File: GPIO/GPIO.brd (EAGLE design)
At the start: 25.4 x 25.4 mm, 11 parts

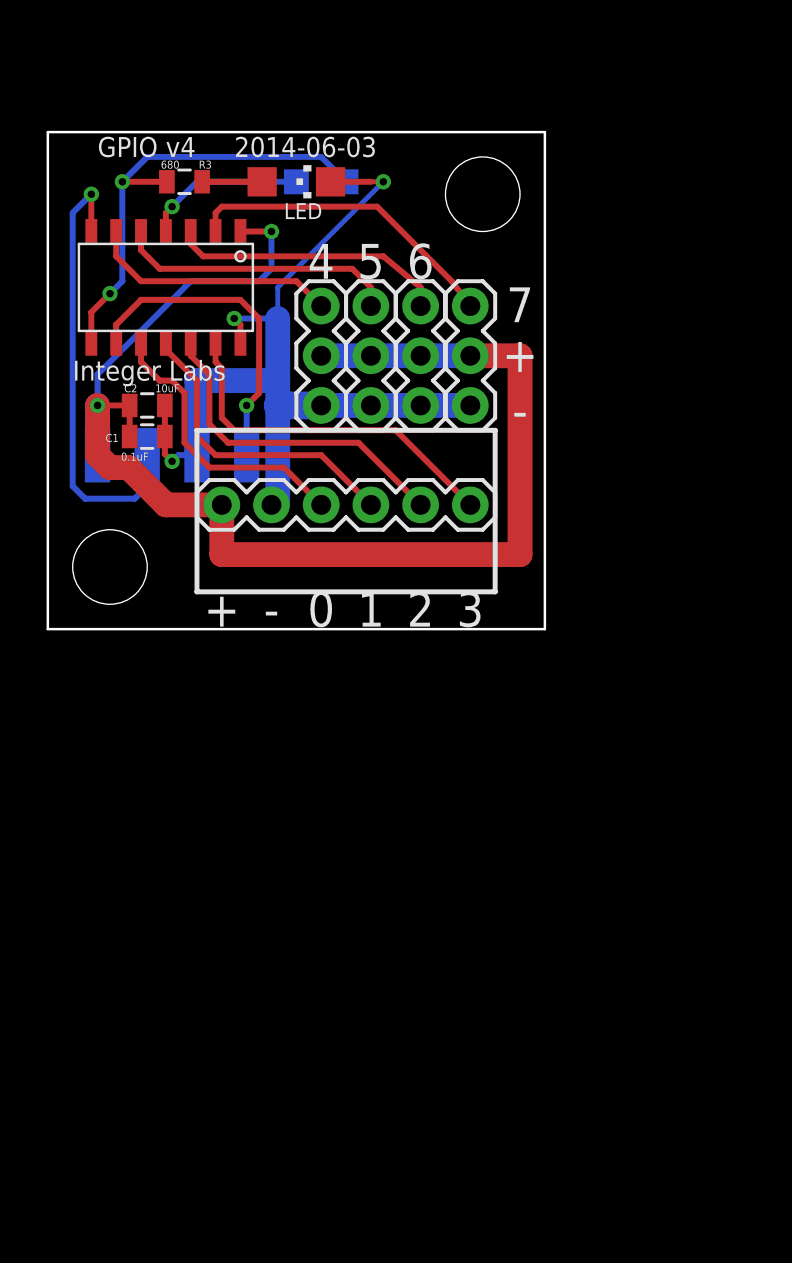
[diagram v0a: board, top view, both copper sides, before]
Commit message: GPIO board rebuilt for v2 footprint
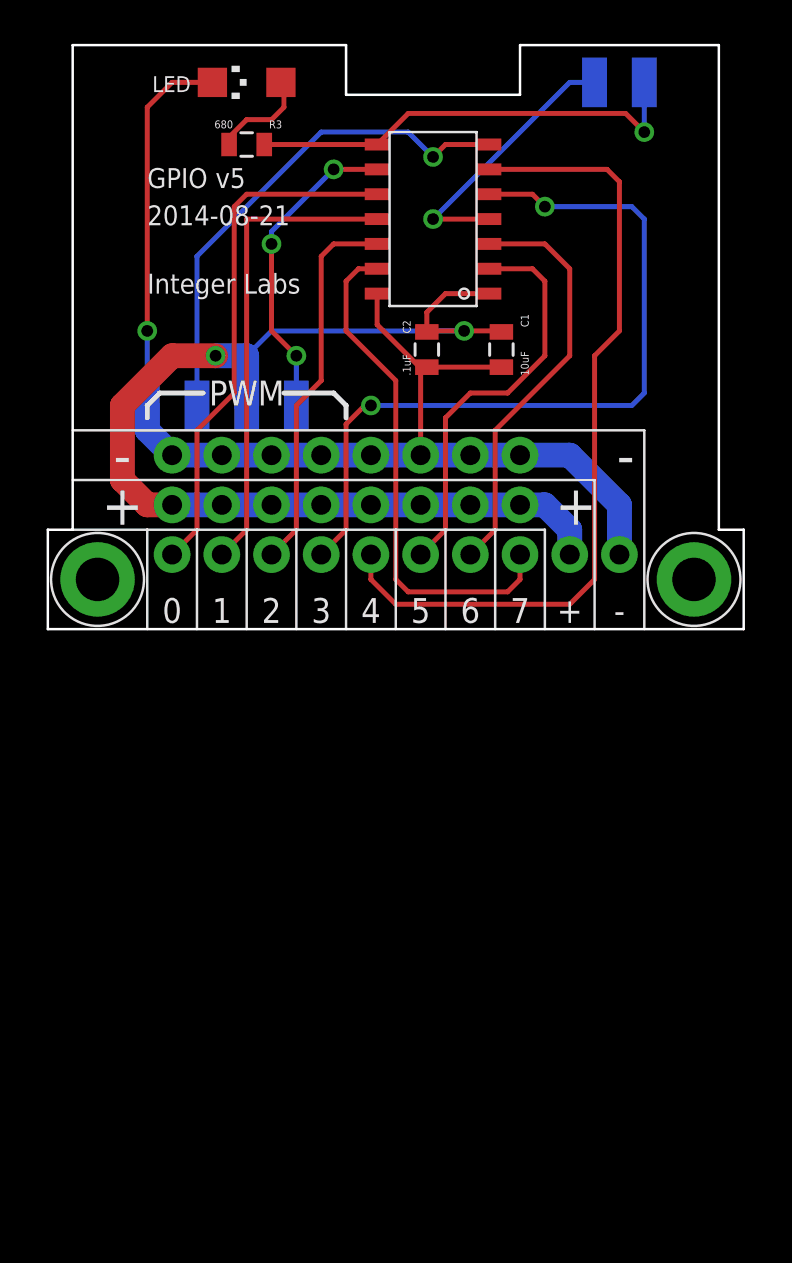
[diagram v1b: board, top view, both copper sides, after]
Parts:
- removed JP5, JP6, JP7, JP8: (no value), SparkFun-Connectors:1X03
- added JP1, JP3: (no value), SparkFun-Connectors:1X08_NO_SILK
- C1: value 0.1uF -> 10uF
- C2: value 10uF -> .1uF
- JP2: value (none) -> M10NO_SILK; device SparkFun-Connectors:1X06 -> SparkFun-Connectors:1X10_NO_SILK
- U$4: value FOOTPRINT -> FOOTPRINTFOOTPRINT-2; device IntegerLabs:FOOTPRINT -> IntegerLabs:FOOTPRINT2
- moved C1 18.6 mm to (23.2, 14.3), turned to 90 degrees
- moved C2 14.6 mm to (19.4, 14.3), turned to 90 degrees
- moved U$3 9.53 mm to (19.4, 17.1), turned to 90 degrees
- moved LED 5.68 mm to (10.2, 27.9), turned to 90 degrees
- moved R3 3.70 mm to (10.2, 24.8), turned to 0 degrees
- moved JP2 3.59 mm to (6.35, 3.81)
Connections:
- net GND: now also JP1.1, JP1.2, JP1.3, JP1.4, JP1.5, JP1.6, JP1.7, JP1.8, JP2.10, U$4.GND; no longer JP2.2, JP5.3, JP6.3, JP7.3, JP8.3, U$4.P$3
- net GPIO0: now also JP2.1; no longer JP2.3
- net GPIO1: now also JP2.2; no longer JP2.4
- net GPIO2: now also JP2.3; no longer JP2.5
- net GPIO3: now also JP2.4, U$3.5; no longer JP2.6, U$3.13
- net GPIO4: now also JP2.5; no longer JP5.1
- net GPIO5: now also JP2.6, U$3.2; no longer JP6.1, U$3.5
- net GPIO6: now also JP2.7; no longer JP7.1
- net GPIO7: now also JP2.8, U$3.13; no longer JP8.1, U$3.2
- net SCL/SCK: now also U$4.SCL; no longer U$4.P$4
- net SDA/MOSI: now also U$4.SDA; no longer U$4.P$2
- net VCC: now also JP2.9, JP3.1, JP3.2, JP3.3, JP3.4, JP3.5, JP3.6, JP3.7, JP3.8, U$4.VCC; no longer JP2.1, JP5.2, JP6.2, JP7.2, JP8.2, U$4.P$1
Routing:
- net GPIO4: track 12.8 -> 41.5 mm
- net GPIO3: track 18.5 -> 40.4 mm, vias 0 -> 2
- net GND: track 47.4 -> 62.1 mm, vias 3 -> 1
- net GPIO0: track 14.7 -> 26.7 mm
- net VCC: track 70.0 -> 59.0 mm
- net GPIO7: track 16.3 -> 26.3 mm
- net GPIO1: track 15.8 -> 24.3 mm
- net GPIO6: track 14.2 -> 21.4 mm
- net GPIO5: track 14.4 -> 20.8 mm
- net RESET: track 8.28 -> 14.0 mm
- net SDA/MOSI: track 23.1 -> 26.0 mm
- net GPIO2: track 17.0 -> 19.4 mm
- net N$5: track 3.06 -> 5.15 mm
- net MISO/LED: track 23.7 -> 23.0 mm, vias 2 -> 1
- net SCL/SCK: track 16.4 -> 16.1 mm, vias 1 -> 3
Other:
- board size 25.4 x 25.4 mm -> 35.6 x 29.8 mm
- board text added: "2014-08-21"
- board text added: "GPIO v5"
- board text added: "PWM"
- board text removed: "2014-06-03"
- board text removed: "GPIO v4"

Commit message: Added current limiting resistors to io pins
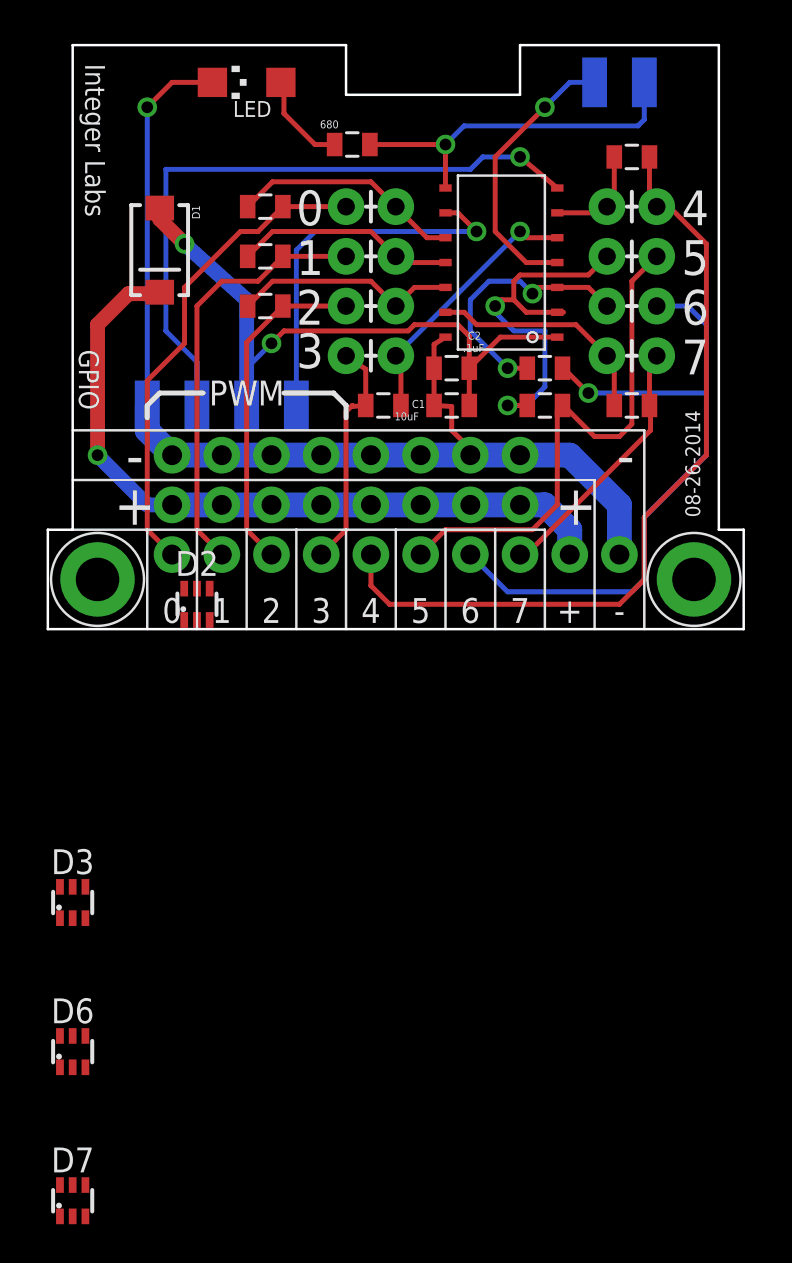
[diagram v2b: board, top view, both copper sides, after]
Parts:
- removed R3: 680, SparkFun-Passives:0805
- added D1: DIODE-SCHOTTKY_, SparkFun-DiscreteSemi:SMA-DIODE
- added D2, D3, D6, D7: BAS70XY, diode:SOT363_PHILIPS
- added R0A, R1A, R2A, R3A, R4A, R5A, R6A, R7A: (no value), SparkFun-Resistors:AXIAL-0.1
- added R0B, R1B, R2B, R3B, R4B, R5B, R6B, R7B: (no value), SparkFun-Resistors:0805
- added RLED: 680, SparkFun-Passives:0805
- moved U$3 4.14 mm to (22.9, 14.9)
- moved C2 3.13 mm to (20.6, 11.4), turned to 0 degrees
- moved C1 2.71 mm to (20.6, 13.3), turned to 0 degrees
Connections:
- new net N$1: D2.2, D6.6
- new net N$2: D2.5, D6.3
- new net N$3: D3.2, D7.6
- new net P0: JP2.1, R0A.P$2, R0B.2
- new net P1: JP2.2, R1A.P$2, R1B.2
- new net P2: JP2.3, R2A.P$2, R2B.2
- new net P3: JP2.4, R3A.P$2, R3B.2
- new net P4: JP2.5, R4A.P$1, R4B.1
- new net P5: JP2.6, R5A.P$1, R5B.1
- new net P6: JP2.7, R6A.P$1, R6B.1
- new net P7: JP2.8, R7A.P$1, R7B.1
- new net VOUT: D1.C, JP2.9, JP3.1, JP3.2, JP3.3, JP3.4, JP3.5, JP3.6, JP3.7, JP3.8
- net GPIO0: now also R0A.P$1, R0B.1; no longer JP2.1
- net GPIO1: now also R1A.P$1, R1B.1; no longer JP2.2
- net GPIO2: now also R2A.P$1, R2B.1; no longer JP2.3
- net GPIO3: now also R3A.P$1, R3B.1; no longer JP2.4
- net GPIO4: now also R4A.P$2, R4B.2; no longer JP2.5
- net GPIO5: now also R5A.P$2, R5B.2; no longer JP2.6
- net GPIO6: now also R6A.P$2, R6B.2; no longer JP2.7
- net GPIO7: now also R7A.P$2, R7B.2; no longer JP2.8
- net MISO/LED: now also RLED.2; no longer R3.2
- net N$5: now also RLED.1; no longer R3.1
- net VCC: now also D1.A; no longer JP2.9, JP3.1, JP3.2, JP3.3, JP3.4, JP3.5, JP3.6, JP3.7, JP3.8
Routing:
- net P4: track 0.00 -> 41.0 mm
- net VOUT: track 0.00 -> 37.5 mm, vias 0 -> 1
- net GPIO4: track 41.5 -> 5.36 mm
- net P6: track 0.00 -> 35.1 mm, vias 0 -> 1
- net GPIO3: track 40.4 -> 13.6 mm, vias 2 -> 1
- net P5: track 0.00 -> 26.8 mm
- net P0: track 0.00 -> 24.9 mm
- net VCC: track 59.0 -> 35.2 mm
- net P1: track 0.00 -> 21.9 mm
- net P2: track 0.00 -> 17.2 mm
- net GPIO0: track 26.7 -> 11.8 mm
- net GPIO7: track 26.3 -> 11.9 mm
- net P7: track 0.00 -> 13.3 mm
- net GPIO1: track 24.3 -> 11.3 mm
- net P3: track 0.00 -> 12.1 mm
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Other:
- board text added: "08-26-2014"
- board text added: "GPIO"
- board text removed: "2014-08-21"
- board text removed: "GPIO v5"

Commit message: Ruggedized GPIO board with current limiting resistors and clamping diodes.
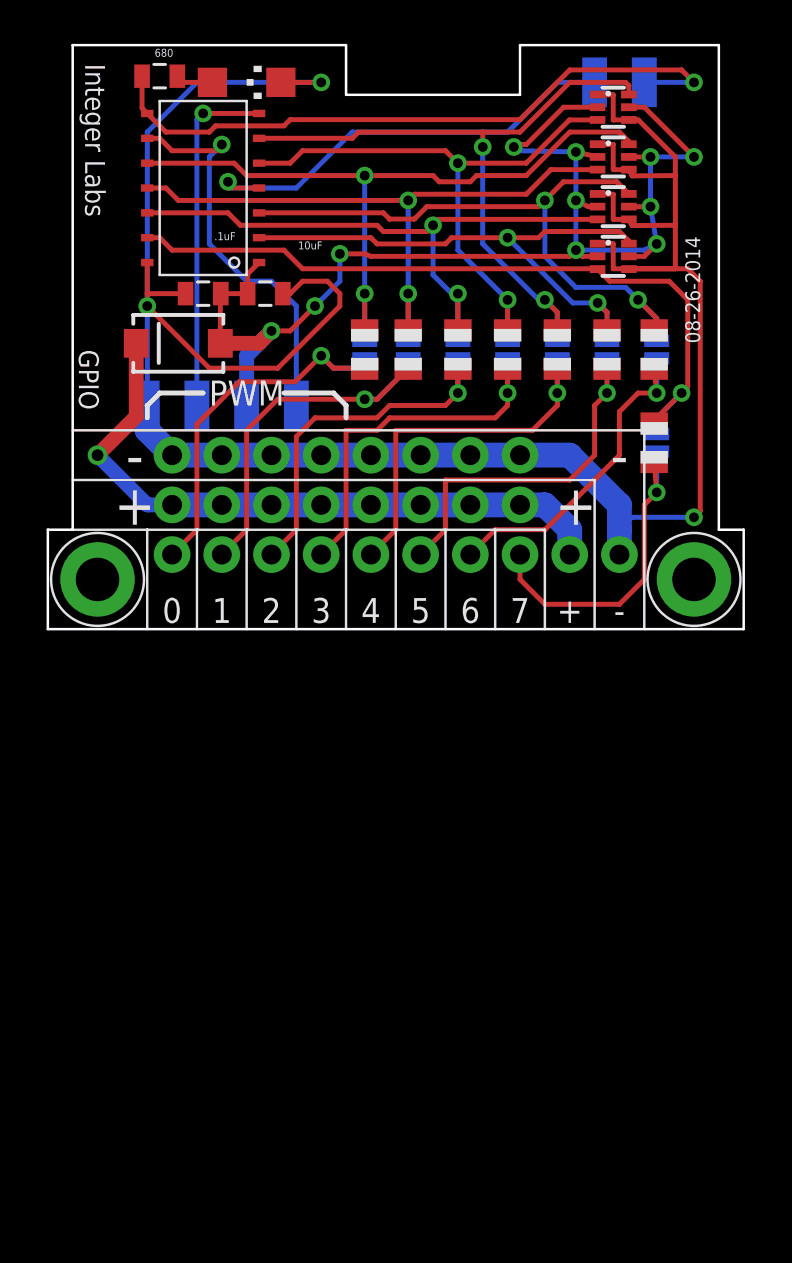
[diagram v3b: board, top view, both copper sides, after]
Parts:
- removed D2, D6: BAS70XY, diode:SOT363_PHILIPS
- removed R0A, R1A, R2A, R3A, R4A, R5A, R6A, R7A: (no value), SparkFun-Resistors:AXIAL-0.1
- removed R0B, R1B, R2B, R3B, R4B, R5B, R6B, R7B: (no value), SparkFun-Resistors:0805
- added D0, D5: BAS70XY, diode:SOT363_PHILIPS
- added R0, R1, R2, R3, R4, R5, R6, R7: SOLDERJUMPERNO, SparkFun-Passives:SJ_2S-NO
- added R10, R11, R12, R13, R14, R15, R8, R9: (no value), adafruit:R0805
- moved D7 55.6 mm to (28.9, 19.1), turned to 270 degrees
- moved D3 47.1 mm to (28.9, 24.1), turned to 270 degrees
- moved U$3 15.7 mm to (7.62, 18.7)
- moved C2 13.9 mm to (7.94, 17.1)
- moved RLED 10.4 mm to (5.71, 28.3), turned to 180 degrees
- moved C1 10.3 mm to (11.1, 17.1), turned to 180 degrees
- moved D1 4.86 mm to (6.67, 14.6), turned to 180 degrees
- turned LED to 270 degrees
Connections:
- removed net N$1: D2.2, D6.6
- removed net N$2: D2.5, D6.3
- removed net N$3: D3.2, D7.6
- net GND: now also D0.1, D0.4, D3.1, D3.4, D5.1, D5.4, D7.1, D7.4
- net GPIO0: now also D3.6, R15.2, R2.1; no longer R0A.P$1, R0B.1
- net GPIO1: now also D3.3, R14.2, R3.1; no longer R1A.P$1, R1B.1
- net GPIO2: now also D5.3, R13.2, R5.1; no longer R2A.P$1, R2B.1
- net GPIO3: now also D0.3, R1.1, R12.2; no longer R3A.P$1, R3B.1
- net GPIO4: now also D0.6, R0.1, R11.2; no longer R4A.P$2, R4B.2
- net GPIO5: now also D7.6, R10.2, R6.1; no longer R5A.P$2, R5B.2
- net GPIO6: now also D5.6, R4.1, R9.2; no longer R6A.P$2, R6B.2
- net GPIO7: now also D7.3, R7.1, R8.2; no longer R7A.P$2, R7B.2
- net P0: now also R15.1, R2.2; no longer R0A.P$2, R0B.2
- net P1: now also R14.1, R3.2; no longer R1A.P$2, R1B.2
- net P2: now also R13.1, R5.2; no longer R2A.P$2, R2B.2
- net P3: now also R1.2, R12.1; no longer R3A.P$2, R3B.2
- net P4: now also R0.2, R11.1; no longer R4A.P$1, R4B.1
- net P5: now also R10.1, R6.2; no longer R5A.P$1, R5B.1
- net P6: now also R4.2, R9.1; no longer R6A.P$1, R6B.1
- net P7: now also R7.2, R8.1; no longer R7A.P$1, R7B.1
- net VCC: now also D0.2, D0.5, D3.2, D3.5, D5.2, D5.5, D7.2, D7.5
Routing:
- net GND: track 56.2 -> 124.7 mm, vias 1 -> 3
- net VCC: track 35.2 -> 67.7 mm, vias 2 -> 11
- net GPIO4: track 5.36 -> 34.8 mm, vias 0 -> 2
- net GPIO7: track 11.9 -> 38.5 mm, vias 0 -> 1
- net GPIO0: track 11.8 -> 36.7 mm, vias 0 -> 2
- net P4: track 41.0 -> 19.3 mm, vias 0 -> 1
- net GPIO1: track 11.3 -> 33.0 mm, vias 0 -> 2
- net GPIO2: track 11.6 -> 32.1 mm, vias 0 -> 2
- net GPIO6: track 13.5 -> 33.0 mm
- net P6: track 35.1 -> 17.2 mm
- net GPIO3: track 13.6 -> 30.4 mm, vias 1 -> 2
- net MISO/LED: track 18.7 -> 34.5 mm
- net SDA/MOSI: track 33.6 -> 17.9 mm
- net GPIO5: track 19.5 -> 29.3 mm
- net RESET: track 14.3 -> 23.2 mm
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
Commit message: Latest version of schematics and boards
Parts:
- removed C1: 10uF, SparkFun-Capacitors:0805
- removed D0, D3, D5, D7: BAS70XY, diode:SOT363_PHILIPS
- added D26, D27, D28, D29: BAS70XY, diode:SOT363_PHILIPS
- C2: value .1uF -> .47uF
- R10, R11, R12, R13, R14, R15, R8, R9: value (none) -> 200; device adafruit:R0805 -> SparkFun-Resistors:0805
- moved LED 7.63 mm to (17.8, 28.3)
- moved R7 4.80 mm to (30.5, 14.3)
- moved R8 4.79 mm to (30.5, 14.3)
- moved R4 2.86 mm to (28.3, 14.3)
- moved R9 2.73 mm to (28.3, 14.3)
- moved R10 2.54 mm to (26.0, 14.3)
- moved R6 2.54 mm to (26.0, 14.3)
- moved R0 2.22 mm to (23.8, 14.3)
- moved R11 2.22 mm to (23.8, 14.3)
- moved R1 1.91 mm to (21.6, 14.3)
- moved R12 1.91 mm to (21.6, 14.3)
- moved R13 1.59 mm to (19.4, 14.3)
- moved R5 1.59 mm to (19.4, 14.3)
- moved R14 1.27 mm to (17.1, 14.3)
- moved R15 1.27 mm to (14.9, 14.3)
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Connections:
- net GND: now also D26.1, D26.4, D27.1, D27.4, D28.1, D28.4, D29.1, D29.4, U$4.BUS0; no longer C1.1, D0.1, D0.4, D3.1, D3.4, D5.1, D5.4, D7.1, D7.4, U$4.GND
- net GPIO0: now also D26.6; no longer D3.6
- net GPIO1: now also D26.3; no longer D3.3
- net GPIO2: now also D27.6; no longer D5.3
- net GPIO3: now also D27.3; no longer D0.3
- net GPIO4: now also D28.6; no longer D0.6
- net GPIO5: now also D28.3; no longer D7.6
- net GPIO6: now also D29.6; no longer D5.6
- net GPIO7: now also D29.3; no longer D7.3
- net MISO/LED: now also U$4.PROG3; no longer U$4.MISO
- net RESET: now also U$4.PROG1; no longer U$4.RESET
- net SCL/SCK: now also U$4.BUS3, U$4.PROG2; no longer U$4.SCL
- net SDA/MOSI: now also U$4.BUS1, U$4.PROG4; no longer U$4.SDA
- net VCC: now also D26.2, D26.5, D27.2, D27.5, D28.2, D28.5, D29.2, D29.5, U$4.BUS2, U$4.PROG0; no longer C1.2, D0.2, D0.5, D3.2, D3.5, D5.2, D5.5, D7.2, D7.5, U$4.VCC
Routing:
- net VCC: track 67.7 -> 87.3 mm
- net SDA/MOSI: track 17.9 -> 35.1 mm, vias 1 -> 2
- net SCL/SCK: track 20.6 -> 34.2 mm, vias 1 -> 2
- net GND: track 124.7 -> 112.0 mm, vias 3 -> 1
- net MISO/LED: track 34.5 -> 23.0 mm
- net RESET: track 23.2 -> 13.5 mm
- net N$5: track 1.93 -> 9.68 mm
- net GPIO4: track 34.8 -> 27.1 mm
- net GPIO2: track 32.1 -> 25.2 mm
- net GPIO6: track 33.0 -> 26.3 mm
- net GPIO3: track 30.4 -> 25.1 mm
- net GPIO0: track 36.7 -> 31.8 mm, vias 2 -> 3
- net GPIO7: track 38.5 -> 42.6 mm, vias 1 -> 2
- net GPIO5: track 29.3 -> 25.8 mm
- net P4: track 19.3 -> 16.8 mm
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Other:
- outline, holes or cut-outs redrawn
- board text added: "I/O"
- board text added: "Modulo"
- board text added: "resistor bypass"
- board text removed: "GPIO"

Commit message: Checkpointing PCB designs
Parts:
- added C1, C3: (no value), SparkFun-Capacitors:1206
- JP2: device SparkFun-Connectors:1X10_NO_SILK -> SparkFun-Connectors:1X08_NO_SILK
- LED: device led:CHIPLED_1206 -> adafruit:CHIPLED_0805
- R10, R11, R12, R13, R14, R15, R8, R9: value 200 -> 130
- moved JP1 7.18 mm to (11.4, 3.81)
- moved JP2 7.18 mm to (11.4, 8.89)
- moved JP3 5.08 mm to (11.4, 6.35)
- moved D1 2.69 mm to (8.57, 12.7), turned to 270 degrees
- moved R0 0.63 mm to (23.8, 14.9)
- moved R1 0.63 mm to (21.6, 14.9)
- moved R10 0.63 mm to (26.0, 14.9)
- moved R11 0.63 mm to (23.8, 14.9)
- moved R12 0.63 mm to (21.6, 14.9)
- moved R13 0.63 mm to (19.4, 14.9)
- moved R14 0.63 mm to (17.1, 14.9)
- moved R15 0.63 mm to (14.9, 14.9)
- moved R2 0.63 mm to (14.9, 14.9)
- moved R3 0.63 mm to (17.1, 14.9)
- moved R4 0.63 mm to (28.3, 14.9)
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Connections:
- net GND: now also C1.1, C3.1; no longer JP2.10
- net VOUT: now also C1.2, C3.2; no longer JP2.9
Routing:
- net P7: track 19.8 -> 7.93 mm
- net P1: track 18.3 -> 8.22 mm
- net P3: track 17.6 -> 7.96 mm
- net P2: track 17.2 -> 8.09 mm
- net P4: track 16.8 -> 7.83 mm
- net P5: track 16.5 -> 7.69 mm
- net P0: track 18.4 -> 9.76 mm
- net GND: track 112.0 -> 120.6 mm, vias 1 -> 3
- net P6: track 15.6 -> 7.56 mm
- net VOUT: track 33.0 -> 29.9 mm
- net GPIO7: track 42.6 -> 41.0 mm
- net VCC: track 87.3 -> 88.3 mm
- net GPIO3: track 25.1 -> 24.2 mm
- net GPIO1: track 30.6 -> 29.8 mm
- net GPIO2: track 25.2 -> 24.5 mm
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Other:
- board size 35.6 x 29.8 mm -> 36.3 x 29.8 mm
- board text removed: "08-26-2014"
- board text removed: "I/O"
- board text removed: "Integer Labs"
- board text removed: "Modulo"
- board text removed: "PWM"
